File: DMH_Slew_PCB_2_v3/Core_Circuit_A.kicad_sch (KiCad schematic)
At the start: 48 parts, among them J1 TS_Jack_6.35mm_Sw, J2 TS_Jack_6.35mm_Sw, J3 TS_Jack_6.35mm_Sw, J50 Conn_01x08_PinHeader, J51 Conn_01x08_PinHeader, Q1 BC548, Q2 BC548, Q3 BC558, Q4 BC558, SW1 SW_DPDT_3way, SW2 SW_DPDT, SW3 SPDT_OnOffOn, U1 TL074, U2 TL074

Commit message: Relinked PCB1 and 2 with new v3 schematics
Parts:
- removed J50, J51: Conn_01x08_PinHeader, Connector_PinSocket_2.54mm:PinSocket_1x08_P2.54mm_Vertical, symbol SynthStuff:Conn_01x08_PinHeader
- added C10, C11, C3, C4: 100nF, Capacitor_THT:C_Disc_D4.3mm_W1.9mm_P5.00mm, symbol Device:C
- added J11, J13, J14, J16: Conn_02x03_Top_Bottom, Connector_PinHeader_2.54mm:PinHeader_2x03_P2.54mm_Horizontal, symbol Connector_Generic:Conn_02x03_Top_Bottom
- added J12, J15: Conn_02x06_Top_Bottom, Connector_PinHeader_2.54mm:PinHeader_2x06_P2.54mm_Horizontal, symbol Connector_Generic:Conn_02x06_Top_Bottom
- added J17, J18: Conn_01x08, Connector_PinHeader_2.54mm:PinHeader_1x08_P2.54mm_Vertical, symbol Connector_Generic:Conn_01x08
- added J19, J20: Conn_01x08, Connector_PinSocket_2.54mm:PinSocket_1x08_P2.54mm_Vertical, symbol Connector_Generic:Conn_01x08
- added unit 5 of U1
- added unit 5 of U2
- Q1, Q3: footprint Package_TO_SOT_THT:TO-92L_Inline_Wide -> Package_TO_SOT_THT:TO-92_Inline
- U1: footprint Package_DIP:DIP-16_W7.62mm_Socket -> Package_DIP:DIP-14_W7.62mm_Socket
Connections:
- net +10V_A: now also J11.2 (Pin_2), J14.2 (Pin_2), J17.5 (Pin_5), J19.5 (Pin_5)
- net GND: now also C10.2, C11.1, C3.2, C4.1, J11.3 (Pin_3), J11.5 (Pin_5), J11.6 (Pin_6), J12.5 (Pin_5), J12.6 (Pin_6), J13.3 (Pin_3), J14.3 (Pin_3), J14.5 (Pin_5), J14.6 (Pin_6), J15.5 (Pin_5), J15.6 (Pin_6), J16.3 (Pin_3), J17.1 (Pin_1), J17.7 (Pin_7), J17.8 (Pin_8), J18.8 (Pin_8), J19.1 (Pin_1), J19.7 (Pin_7), J19.8 (Pin_8), J20.8 (Pin_8)
- net A_Diff_Amp_S: now reaches C6.2, R8.1, U2.1
- net A_Diff_Amp_S: now also J12.1 (Pin_1); no longer SW2.1 (A)
- net A_Rng_Sw_p3_C: now reaches SW3.3 (C)
- net A_Rng_Sw_p3_C: now also J20.5 (Pin_5); no longer C15.2
- net A_LinLog_Sw_p5_S: now reaches R11.2, R12.2
- net A_LinLog_Sw_p5_S: now also J12.7 (Pin_7); no longer SW2.5 (B)
- net A_CV_Buff_C: now reaches SW1.3 (C), SW1.4 (A)
- net A_CV_Buff_C: now also J19.6 (Pin_6); no longer U1.1, U1.2 (-)
- net A_CV_In_Jack_M: now reaches J2.T
- net A_CV_In_Jack_M: now also J16.5 (Pin_5); no longer R1.2
- net A_LinLog_Sw_p2_S: now reaches R10.2, R9.2
- net A_LinLog_Sw_p2_S: now also J12.8 (Pin_8); no longer SW2.2 (B)
- net A_Rng_Sw_p1_C: now reaches SW3.1 (A)
- net A_Rng_Sw_p1_C: now also J20.7 (Pin_7); no longer C14.2
- net Bus CV renamed Bus_CV_M
- net Comp_-R renamed A_Comp_-R
- net Comp_F renamed A_Comp_F
- net Comp_R renamed A_Comp_R
- net Fall_CV renamed A_Fall_CV_C
- net A_Fall_CV_C: now also J19.4 (Pin_4); no longer R23.1
- net Input renamed A_Input_Jack_S
- net A_Input_Jack_S: now also J13.4 (Pin_4); no longer J1.T
- net Out A TN renamed A_Out_Jack_TN_M
- net Output renamed A_Out_Jack_S
- net A_Out_Jack_S: now also J13.6 (Pin_6); no longer J3.T, SW3.2 (B)
- net Rise_CV renamed A_Rise_CV_C
- net A_Rise_CV_C: now also J19.3 (Pin_3); no longer R22.1
- new net +12V: C10.1, C3.1, J11.1 (Pin_1), J14.1 (Pin_1), U1.4 (V+), U2.4 (V+)
- new net -12V: C11.2, C4.2, J11.4 (Pin_4), J14.4 (Pin_4), U1.11 (V-), U2.11 (V-)
- new net A_CV_Buff_M: J15.4 (Pin_4), J17.6 (Pin_6)
- new net A_CV_Buff_S: J12.4 (Pin_4), U1.1, U1.2 (-)
- new net A_CV_In_Jack_S: J13.5 (Pin_5), R1.2
- new net A_Diff_Amp_C: J19.2 (Pin_2), SW2.1 (A)
- new net A_Diff_Amp_M: J15.1 (Pin_1), J17.2 (Pin_2)
- new net A_F_Gate_Jack_M: J16.1 (Pin_1)
- new net A_F_Gate_Jack_S: J13.1 (Pin_1)
- new net A_F_LED_C: J20.4 (Pin_4)
- new net A_F_LED_M: J15.10 (Pin_10), J18.4 (Pin_4)
- new net A_F_LED_S: J12.10 (Pin_10)
- new net A_Fall_CV_M: J15.3 (Pin_3), J17.4 (Pin_4)
- new net A_Fall_CV_S: J12.3 (Pin_3), R23.1
- new net A_Input_Jack_M: J1.T, J16.4 (Pin_4)
- new net A_LinLog_Sw_p2_C: J20.2 (Pin_2), SW2.2 (B)
- new net A_LinLog_Sw_p2_M: J15.8 (Pin_8), J18.2 (Pin_2)
- new net A_LinLog_Sw_p5_C: J20.1 (Pin_1), SW2.5 (B)
- new net A_LinLog_Sw_p5_M: J15.7 (Pin_7), J18.1 (Pin_1)
- new net A_Out_Jack_C: J20.6 (Pin_6), SW3.2 (B)
- new net A_Out_Jack_M: J16.6 (Pin_6), J18.6 (Pin_6), J3.T
- new net A_R_Gate_Jack_M: J16.2 (Pin_2)
- new net A_R_Gate_Jack_S: J13.2 (Pin_2)
- new net A_R_LED_C: J20.3 (Pin_3)
- new net A_R_LED_M: J15.9 (Pin_9), J18.3 (Pin_3)
- new net A_R_LED_S: J12.9 (Pin_9)
- new net A_Rise_CV_M: J15.2 (Pin_2), J17.3 (Pin_3)
- new net A_Rise_CV_S: J12.2 (Pin_2), R22.1
- new net A_Rng_Sw_p1_M: J15.12 (Pin_12), J18.7 (Pin_7)
- new net A_Rng_Sw_p1_S: C14.2, J12.12 (Pin_12)
- new net A_Rng_Sw_p3_M: J15.11 (Pin_11), J18.5 (Pin_5)
- new net A_Rng_Sw_p3_S: C15.2, J12.11 (Pin_11)
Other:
- note removed: "PCB 2"
- moved on the sheet: C14, C15, C6, C7, C8, C9, J1, J2, J3, Q1, Q2, Q3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

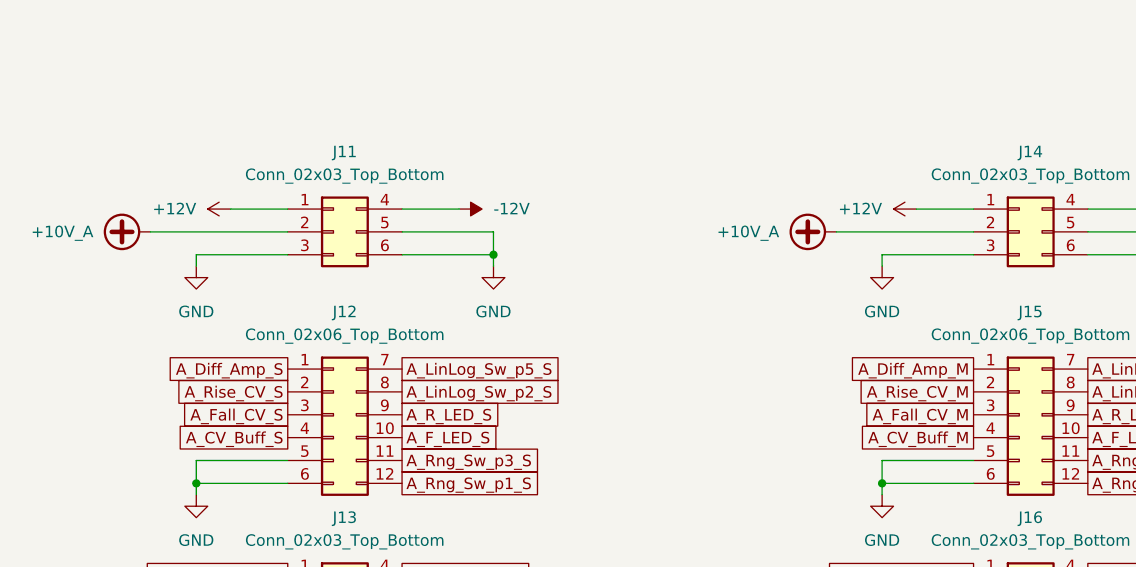
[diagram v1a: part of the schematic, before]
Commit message: PCB 1 routing in progress
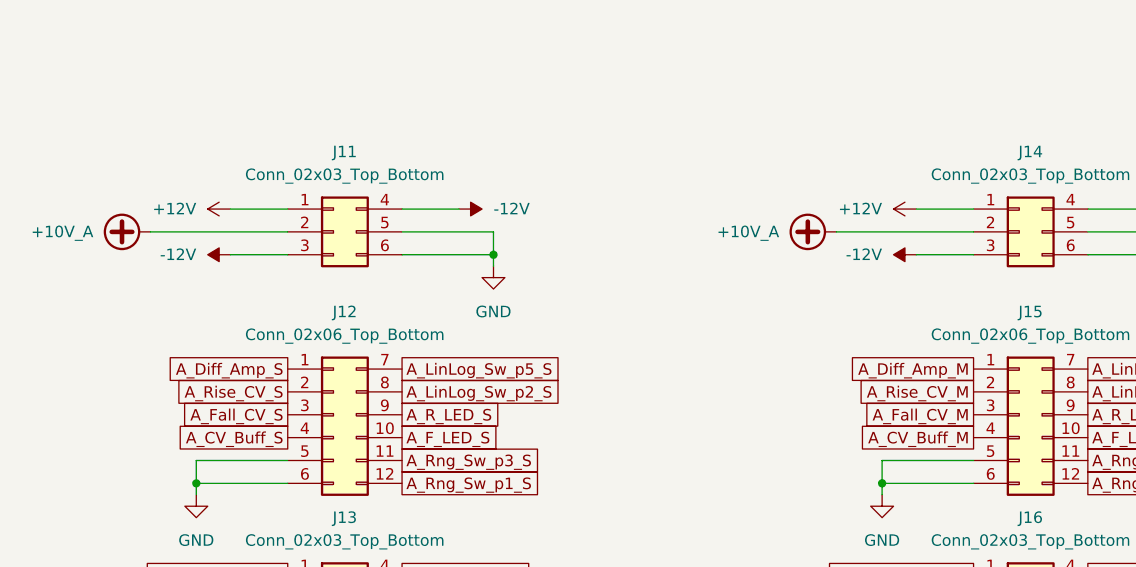
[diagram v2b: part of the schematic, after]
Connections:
- net -12V: now also J11.3 (Pin_3), J14.3 (Pin_3)
- net GND: no longer J11.3 (Pin_3), J14.3 (Pin_3)
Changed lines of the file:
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@@
 	(wire
 		(pts
-			(xy 34.29 231.14) (xy 44.45 231.14)
+			(xy 38.1 231.14) (xy 44.45 231.14)
 		)
 		(stroke
@@
 	(wire
 		(pts
-			(xy 34.29 232.41) (xy 34.29 231.14)
-		)
-		(stroke
-			(width 0)
-			(type default)
-		)
-	)
-	(wire
-		(pts
 			(xy 129.54 74.93) (xy 129.54 72.39)
 		)
@@
 	(wire
 		(pts
-			(xy 120.65 231.14) (xy 110.49 231.14)
+			(xy 120.65 231.14) (xy 114.3 231.14)
 		)
 		(stroke
@@
 	(wire
 		(pts
-			(xy 110.49 231.14) (xy 110.49 232.41)
-		)
-		(stroke
-			(width 0)
-			(type default)
-		)
-	)
-	(wire
-		(pts
 			(xy 165.1 67.31) (xy 167.64 67.31)
 		)
@@
 	)
 	(symbol
-		(lib_id "power:GND")
-		(at 110.49 232.41 0)
-		(unit 1)
-		(exclude_from_sim no)
-		(in_bom yes)
-		(on_board no)
-		(dnp no)
-		(fields_autoplaced yes)
-		(property "Reference" "#PWR091"
-			(at 110.49 238.76 0)
-			(effects
-				(font
-					(size 1.27 1.27)
-				)
-				(hide yes)
-			)
-		)
-		(property "Value" "GND"
-			(at 110.49 237.49 0)
-			(effects
-				(font
-					(size 1.27 1.27)
-				)
-			)
-		)
-		(property "Footprint" ""
-			(at 110.49 232.41 0)
-			(effects
-				(font
-					(size 1.27 1.27)
-				)
-				(hide yes)
-			)
-		)
-		(property "Datasheet" ""
-			(at 110.49 232.41 0)
-			(effects
-				(font
-					(size 1.27 1.27)
-				)
-				(hide yes)
-			)
-		)
-		(property "Description" "Power symbol creates a global label with name \"GND\" , ground"
-			(at 110.49 232.41 0)
-			(effects
-				(font
-					(size 1.27 1.27)
-				)
-				(hide yes)
-			)
-		)
-		(pin "1"
-		)
-		(instances
-			(project "DMH_Slew_PCB_2_v3"
-				(path "/58f4306d-5387-4983-bb08-41a2313fd315/7ad2d702-dfb7-4d49-a82d-34430dd5948f"
-					(reference "#PWR091")
-					(unit 1)
-				)
-			)
-		)
-	)
-	(symbol
 		(lib_id "Transistor_BJT:BC558")
 		(at 228.6 173.99 270)
@@
 	)
 	(symbol
+		(lib_id "power:-12V")
+		(at 114.3 231.14 90)
+		(unit 1)
+		(exclude_from_sim no)
+		(in_bom yes)
+		(on_board no)
+		(dnp no)
+		(fields_autoplaced yes)
+		(property "Reference" "#PWR091"
+			(at 118.11 231.14 0)
+			(effects
+				(font
+					(size 1.27 1.27)
+				)
+				(hide yes)
+			)
+		)
+		(property "Value" "-12V"
+			(at 110.49 231.1399 90)
+			(effects
+				(font
+					(size 1.27 1.27)
+				)
+				(justify left)
+			)
+		)
+		(property "Footprint" ""
+			(at 114.3 231.14 0)
+			(effects
+				(font
+					(size 1.27 1.27)
+				)
+				(hide yes)
+			)
+		)
+		(property "Datasheet" ""
+			(at 114.3 231.14 0)
+			(effects
+				(font
+					(size 1.27 1.27)
+				)
+				(hide yes)
+			)
+		)
+		(property "Description" "Power symbol creates a global label with name \"-12V\""
+			(at 114.3 231.14 0)
+			(effects
+				(font
+					(size 1.27 1.27)
+				)
+				(hide yes)
+			)
+		)
+		(pin "1"
+		)
+		(instances
+			(project "DMH_Slew_PCB_2_v3"
+				(path "/58f4306d-5387-4983-bb08-41a2313fd315/7ad2d702-dfb7-4d49-a82d-34430dd5948f"
+					(reference "#PWR091")
+					(unit 1)
+				)
+			)
+		)
+	)
+	(symbol
 		(lib_id "Device:C")
 		(at 279.4 67.31 90)
@@
 	)
 	(symbol
+		(lib_id "power:-12V")
+		(at 38.1 231.14 90)
+		(unit 1)
+		(exclude_from_sim no)
+		(in_bom yes)
+		(on_board no)
+		(dnp no)
+		(fields_autoplaced yes)
+		(property "Reference" "#PWR087"
+			(at 41.91 231.14 0)
+			(effects
+				(font
+					(size 1.27 1.27)
+				)
+				(hide yes)
+			)
+		)
+		(property "Value" "-12V"
+			(at 34.29 231.1399 90)
+			(effects
+				(font
+					(size 1.27 1.27)
+				)
+				(justify left)
+			)
+		)
+		(property "Footprint" ""
+			(at 38.1 231.14 0)
+			(effects
+				(font
+					(size 1.27 1.27)
+				)
+				(hide yes)
+			)
+		)
+		(property "Datasheet" ""
+			(at 38.1 231.14 0)
+			(effects
+				(font
+					(size 1.27 1.27)
+				)
+				(hide yes)
+			)
+		)
+		(property "Description" "Power symbol creates a global label with name \"-12V\""
+			(at 38.1 231.14 0)
+			(effects
+				(font
+					(size 1.27 1.27)
+				)
+				(hide yes)
+			)
+		)
+		(pin "1"
+		)
+		(instances
+			(project "DMH_Slew_PCB_2_v3"
+				(path "/58f4306d-5387-4983-bb08-41a2313fd315/7ad2d702-dfb7-4d49-a82d-34430dd5948f"
+					(reference "#PWR087")
+					(unit 1)
+				)
+			)
+		)
+	)
+	(symbol
 		(lib_id "power:GND")
 		(at 317.5 232.41 0)
@@
 					(unit 1)
 				)
-			)
-		)
-	)
-	(symbol
-		(lib_id "power:GND")
-		(at 34.29 232.41 0)
-		(mirror y)
-		(unit 1)
-		(exclude_from_sim no)
-		(in_bom yes)
-		(on_board no)
-		(dnp no)
-		(fields_autoplaced yes)
-		(property "Reference" "#PWR087"
-			(at 34.29 238.76 0)
-			(effects
-				(font
-					(size 1.27 1.27)
-				)
-				(hide yes)
-			)
-		)
-		(property "Value" "GND"
-			(at 34.29 237.49 0)
-			(effects
-				(font
-					(size 1.27 1.27)
-				)
-			)
-		)
-		(property "Footprint" ""
-			(at 34.29 232.41 0)
-			(effects
-				(font
-					(size 1.27 1.27)
-				)
-				(hide yes)
-			)
-		)
-		(property "Datasheet" ""
-			(at 34.29 232.41 0)
-			(effects
-				(font
-					(size 1.27 1.27)
-				)
-				(hide yes)
-			)
-		)
-		(property "Description" "Power symbol creates a global label with name \"GND\" , ground"
-			(at 34.29 232.41 0)
-			(effects
-				(font
-					(size 1.27 1.27)
-				)
-				(hide yes)
-			)
-		)
-		(pin "1"
-		)
-		(instances
-			(project "DMH_Slew_PCB_2_v3"
-				(path "/58f4306d-5387-4983-bb08-41a2313fd315/7ad2d702-dfb7-4d49-a82d-34430dd5948f"
-					(reference "#PWR087")
-					(unit 1)
-				)
